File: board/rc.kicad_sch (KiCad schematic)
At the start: 42 parts, among them IC1 A3909GLNTR-T, J1 Conn_01x24, J2 Conn_01x06, Q1 Q_NPN_BEC, Q2 Q_NPN_BEC, U1 ESP32-S3-MINI-1U, U2 TPS560430YDBVR, U3 XC6206PxxxMR, U4 XC6206PxxxMR

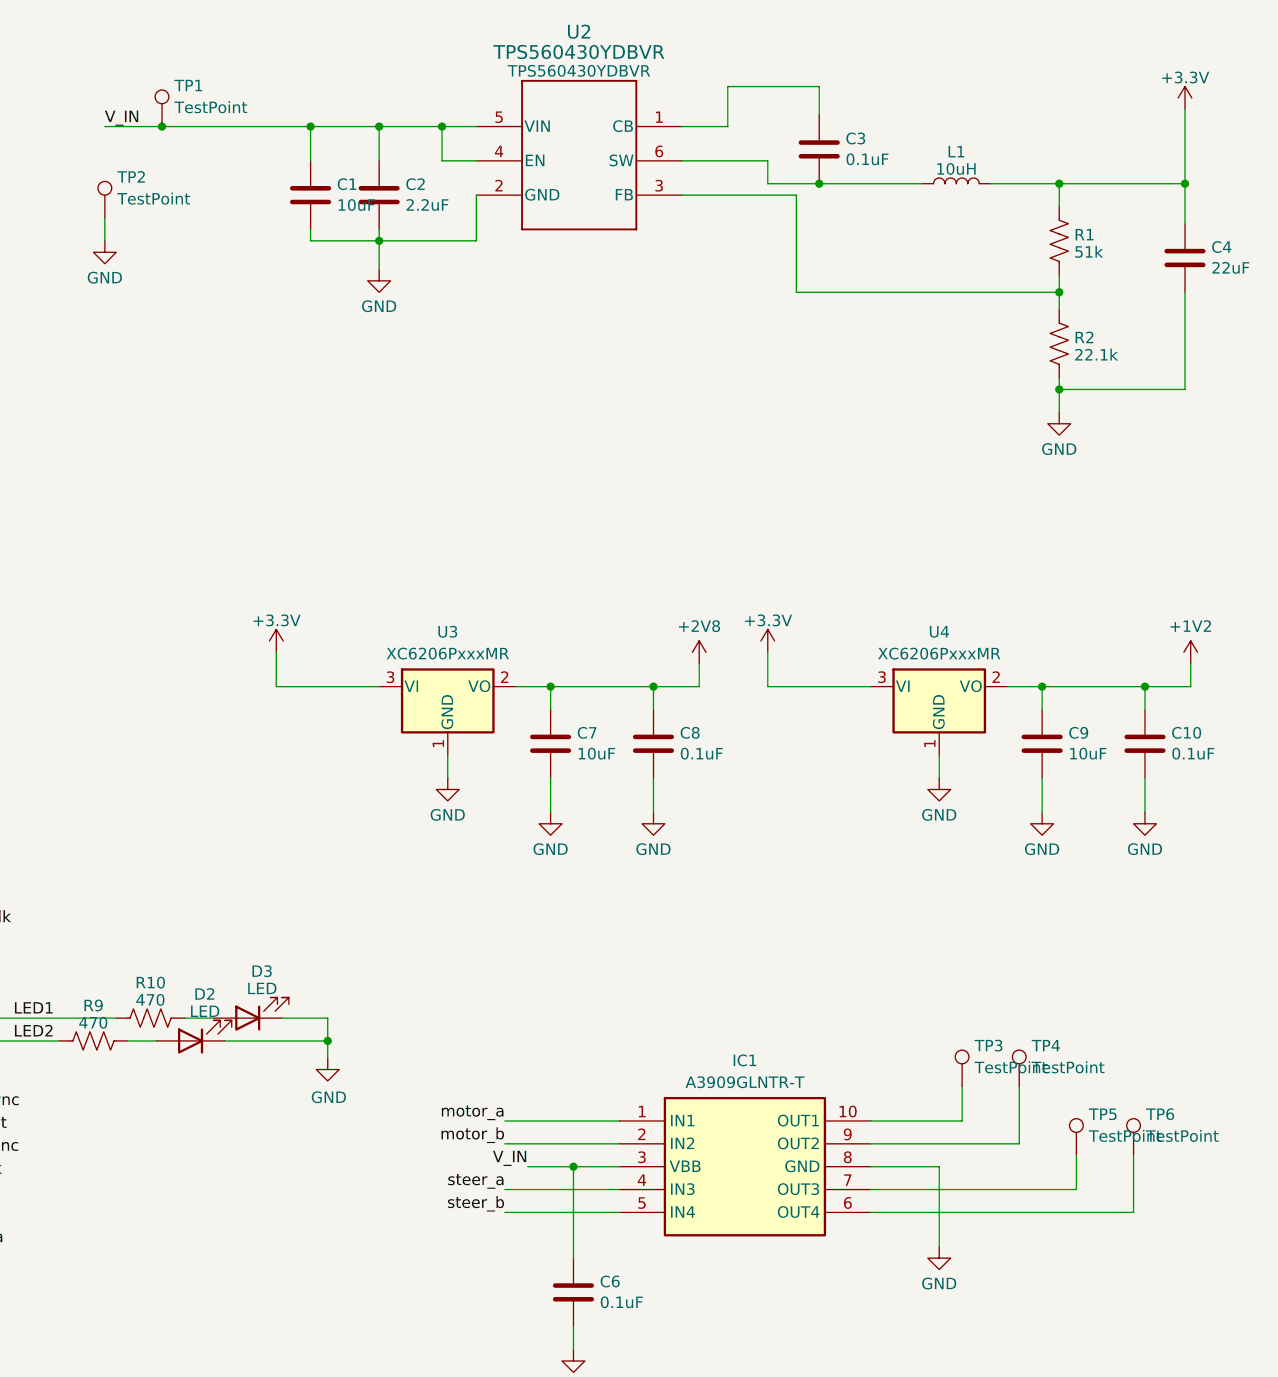
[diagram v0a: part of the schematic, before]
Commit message: added another motor driver, made mounting holes smaller, added cap for input voltage
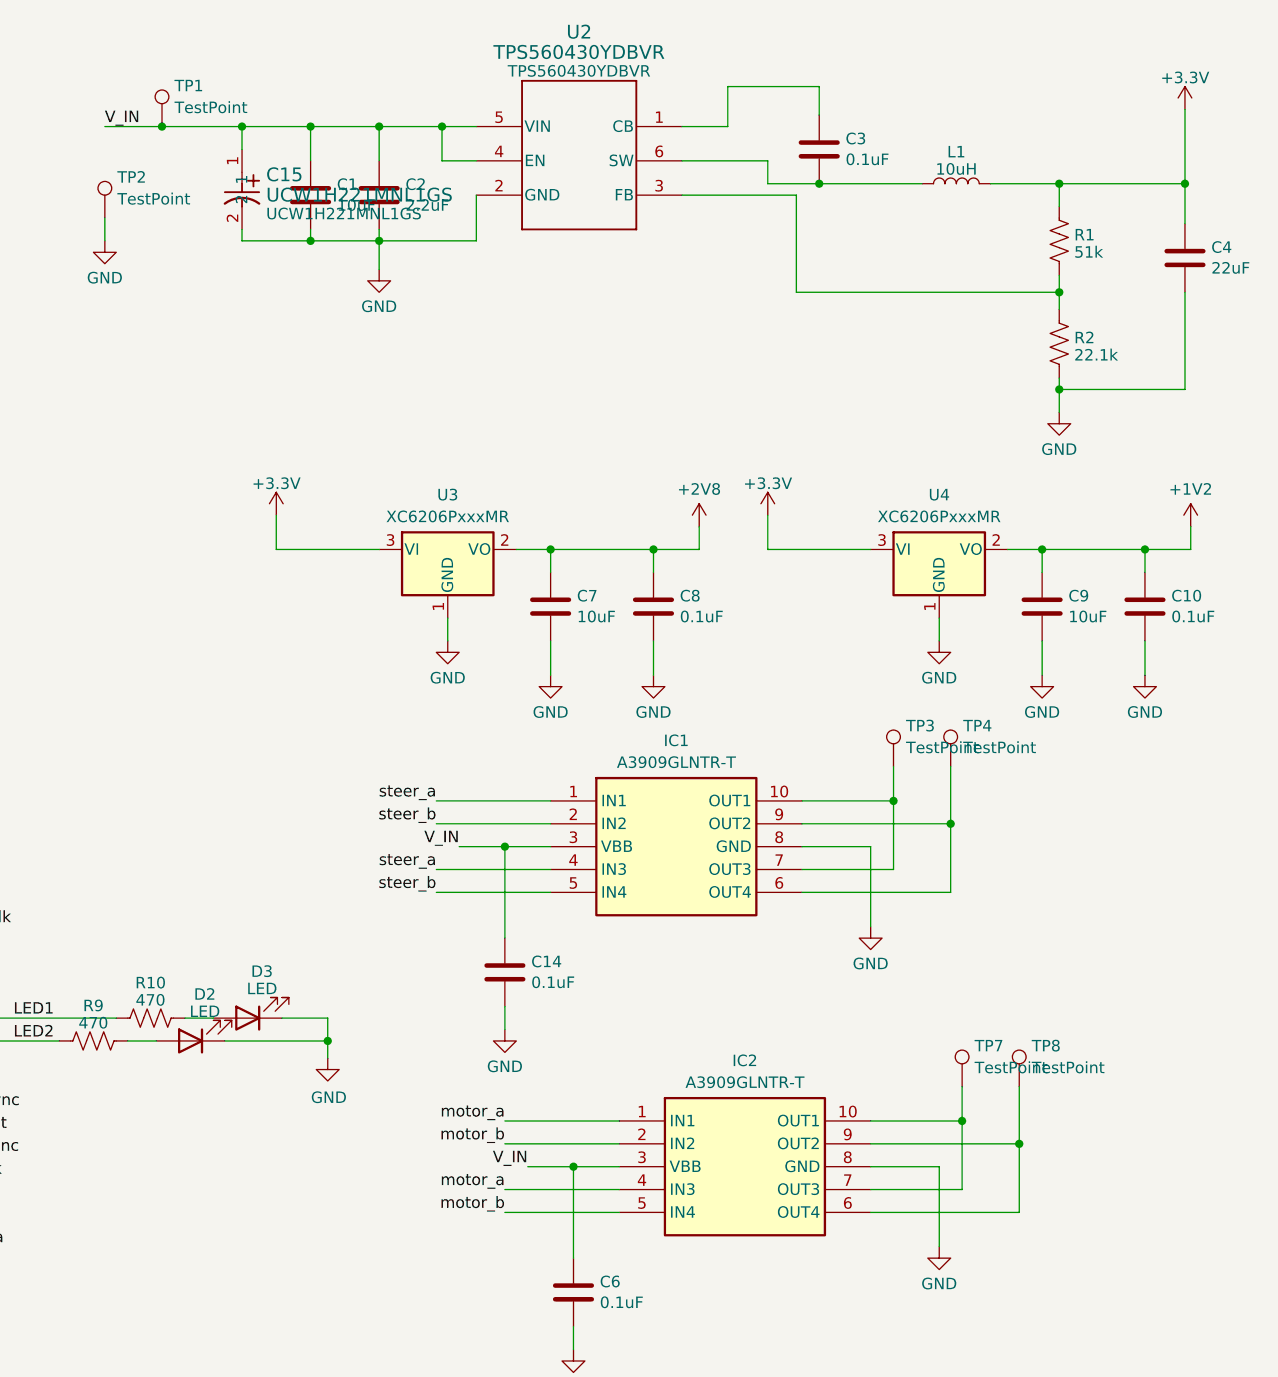
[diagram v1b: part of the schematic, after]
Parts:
- removed TP5, TP6: TestPoint, MountingHole:MountingHole_2.2mm_M2_ISO7380_Pad_TopBottom, symbol Connector:TestPoint
- added C14: 0.1uF, Capacitor_SMD:C_0603_1608Metric, symbol Device:C
- added C15: UCW1H221MNL1GS, footprints2:UCW1H221MNL1GS, symbol MyLibrary:UCW1H221MNL1GS
- added IC2: A3909GLNTR-T, footprints:SOP100P600X175-10N, symbol mylibrary:A3909GLNTR-T
- added TP7, TP8: TestPoint, MountingHole:MountingHole_2.2mm_M2_ISO7380_Pad_TopBottom, symbol Connector:TestPoint
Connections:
- net GND: now also C14.2, C15.2, IC2.8 (GND)
- net V_IN: now also C14.1, C15.1, IC2.3 (VBB)
- net motor_a: now also IC2.1 (IN1), IC2.4 (IN3); no longer IC1.1 (IN1)
- net motor_b: now also IC2.2 (IN2), IC2.5 (IN4); no longer IC1.2 (IN2)
- net steer_a: now also IC1.1 (IN1)
- net steer_b: now also IC1.2 (IN2)
- net at IC1.10 (OUT1), TP3.1: now also IC1.7 (OUT3)
- net at IC1.6 (OUT4): now also IC1.9 (OUT2), TP4.1
- new net: IC2.10 (OUT1), IC2.7 (OUT3), TP7.1
- new net: IC2.6 (OUT4), IC2.9 (OUT2), TP8.1
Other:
- moved on the sheet: C10, C7, C8, C9, IC1, TP3, TP4, U3, U4
